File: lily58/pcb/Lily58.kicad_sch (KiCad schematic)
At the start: 84 parts, among them J1 LED, J2 4PIN, P1 i2c_pin, P2 i2c_pin, P3 ICSP, P4 OLED, SW1 SW_PUSH, SW10 SW_PUSH, SW11 SW_PUSH, SW12 SW_PUSH, SW13 SW_PUSH, SW14 SW_PUSH, SW15 SW_PUSH, SW16 SW_PUSH, SW17 SW_PUSH, SW18 SW_PUSH, SW19 SW_PUSH, SW2 SW_PUSH, SW20 SW_PUSH, SW21 SW_PUSH, SW22 SW_PUSH, SW23 SW_PUSH, SW24 SW_PUSH, SW25 SW_PUSH, SW26 SW_PUSH, SW27 SW_PUSH, SW28 SW_PUSH, SW29 SW_PUSH, SW3 SW_PUSH, SW4 SW_PUSH, SW5 SW_PUSH, SW6 SW_PUSH, SW7 SW_PUSH, SW8 SW_PUSH, SW9 SW_PUSH, U1 ProMicro

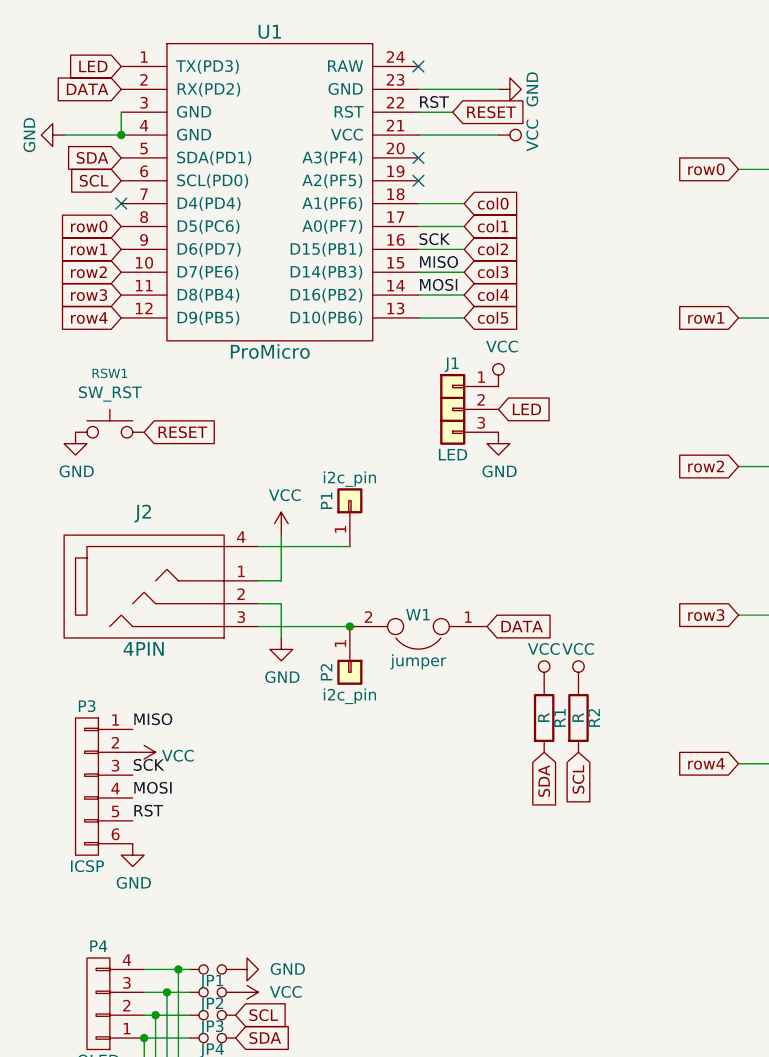
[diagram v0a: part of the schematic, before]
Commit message: lily: fix diode silk screen and remove some unused pads
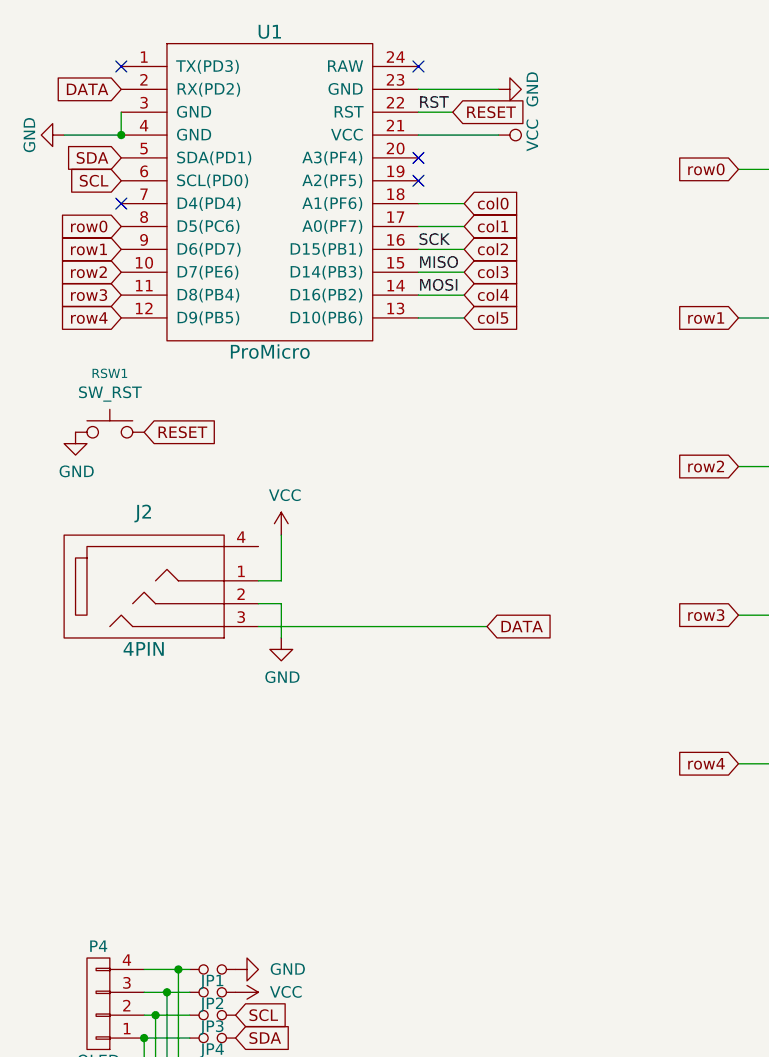
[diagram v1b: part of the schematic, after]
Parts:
- removed J1: LED, Lily58-footprint:StripLED, symbol Lily58-rescue:LED-Lily58-cache
- removed P1, P2: i2c_pin, Lily58-footprint:1pin_conn, symbol Lily58-rescue:i2c_pin-Lily58-cache
- removed P3: ICSP, Lily58-footprint:ICSP, symbol Lily58-rescue:CONN_01X06-Lily58-cache
- removed R1, R2: R, Lily58-footprint:RESISTOR_mini, symbol Lily58-rescue:R-Lily58-cache
- removed W1: jumper, Lily58-footprint:jumper_data, symbol Lily58-rescue:Jumper-Device
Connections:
- net DATA: now also J2.3
- net LED: no longer names the net of U1.1 (TX(PD3))
- no-connect marks 4 -> 5
